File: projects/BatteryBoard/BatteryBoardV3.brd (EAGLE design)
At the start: 90.6 x 96 mm, 231 parts, among them M1 BSO201SP, SW1 BTS50015-1TAD, SW2 BTS50015-1TAD, T1 AD590FLATPACK, T2 AD590FLATPACK, T3 AD590FLATPACK, T4 AD590FLATPACK, U1 TCA9535PWR, U10 LT1962-3, U11 LT1962-3, U12 LTC4411, U13 LTC4411, U14 LTC4121, U16 LTC4121, U18 AD8418, U19 AD8418, U2 AD7991-0, U3 LTC4412MPS6, U4 LTC4121-4.2, U5 LTC4121-4.2, U6 LC05111C13MTTTG, U7 LC05111C13MTTTG, U8 AD8418, U9 AD8418

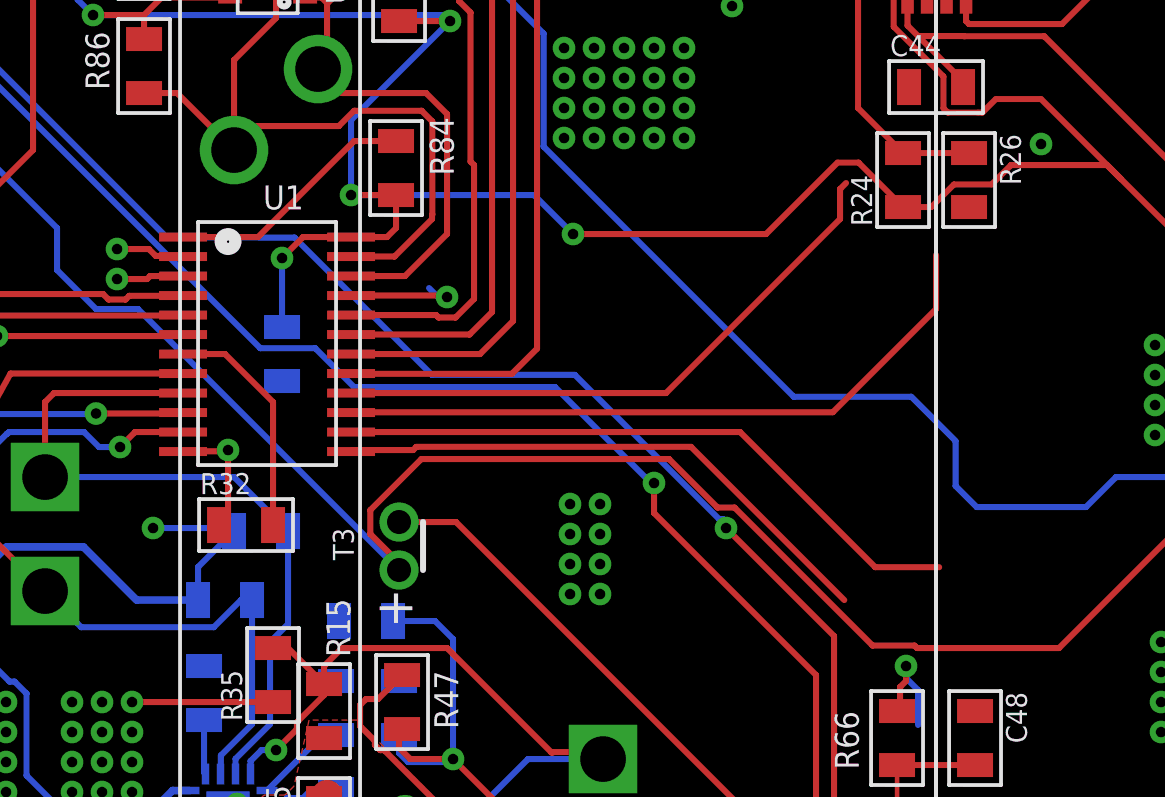
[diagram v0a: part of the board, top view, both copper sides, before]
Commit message: 100K pulldowns for unused GPIO expander pins
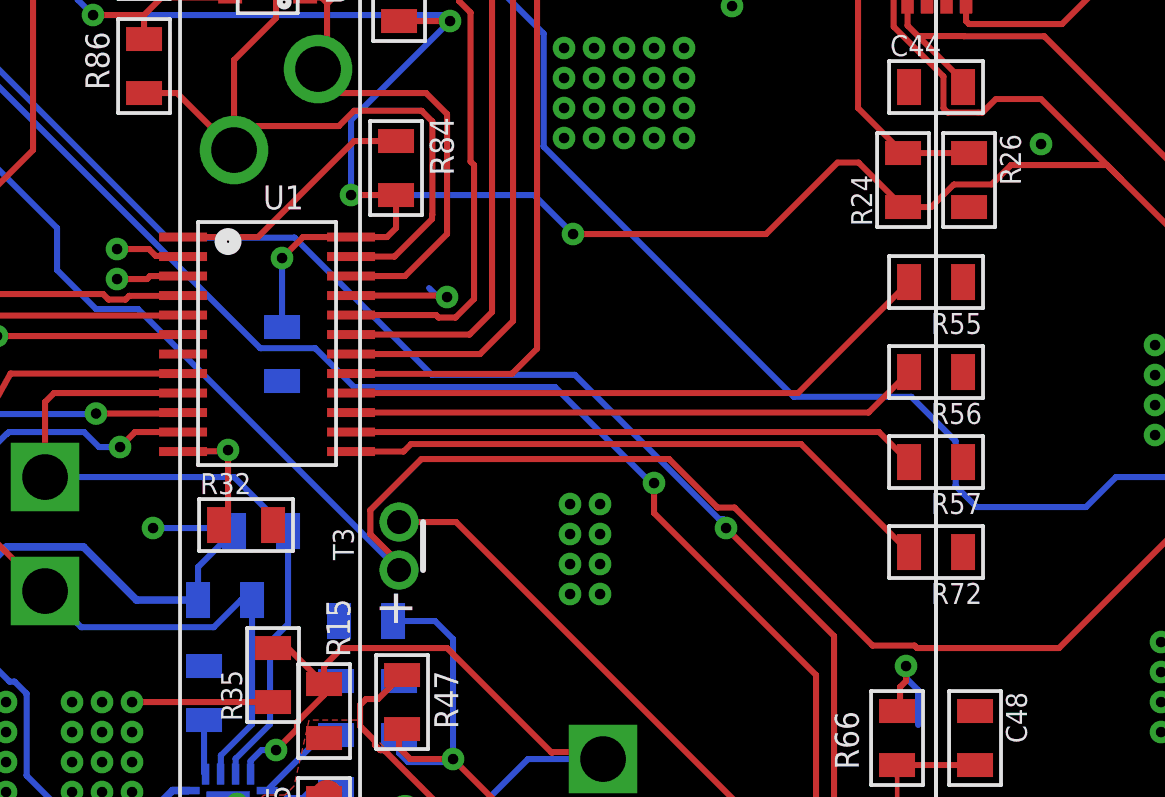
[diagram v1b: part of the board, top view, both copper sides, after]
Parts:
- added R55, R56, R57, R72: 100K, BrownSpaceEngineering:0805
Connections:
- removed net LF_B1_BT: U1.P$16
- removed net LF_B1_TT: U1.P$15
- removed net LF_B2_BT: U1.P$13
- removed net LF_B2_TT: U1.P$14
- new net N$20: R72.2, U1.P$13
- new net N$21: R57.2, U1.P$14
- new net N$23: R56.2, U1.P$15
- new net N$24: R55.2, U1.P$16
- net GND: now also R55.1, R56.1, R57.1, R72.1
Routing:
- net LF_B1_TT: track 22.7 -> 0.00 mm
- net LF_B2_TT: track 21.5 -> 0.00 mm
- net N$20: track 0.00 -> 20.2 mm
- net N$24: track 0.00 -> 20.1 mm
- net LF_B1_BT: track 20.0 -> 0.00 mm
- net N$23: track 0.00 -> 19.2 mm
- net N$21: track 0.00 -> 19.0 mm
- net LF_B2_BT: track 18.6 -> 0.00 mm
- net N$15: track 7.76 -> 0.00 mm
